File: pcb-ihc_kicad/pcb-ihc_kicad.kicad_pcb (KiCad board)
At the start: 2 copper layers, 100 x 160 mm, 76 parts, among them J1 D-IN with pullup, J10 D-IN with pulldown, J11 2x N-Mosfet, J2 Screw_Terminal_01x01, J3 Screw_Terminal_01x01, J4 Screw_Terminal_01x01, J5 Screw_Terminal_01x01, J6 Screw_Terminal_01x01, J7 Screw_Terminal_01x01, J8 Screw_Terminal_01x01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

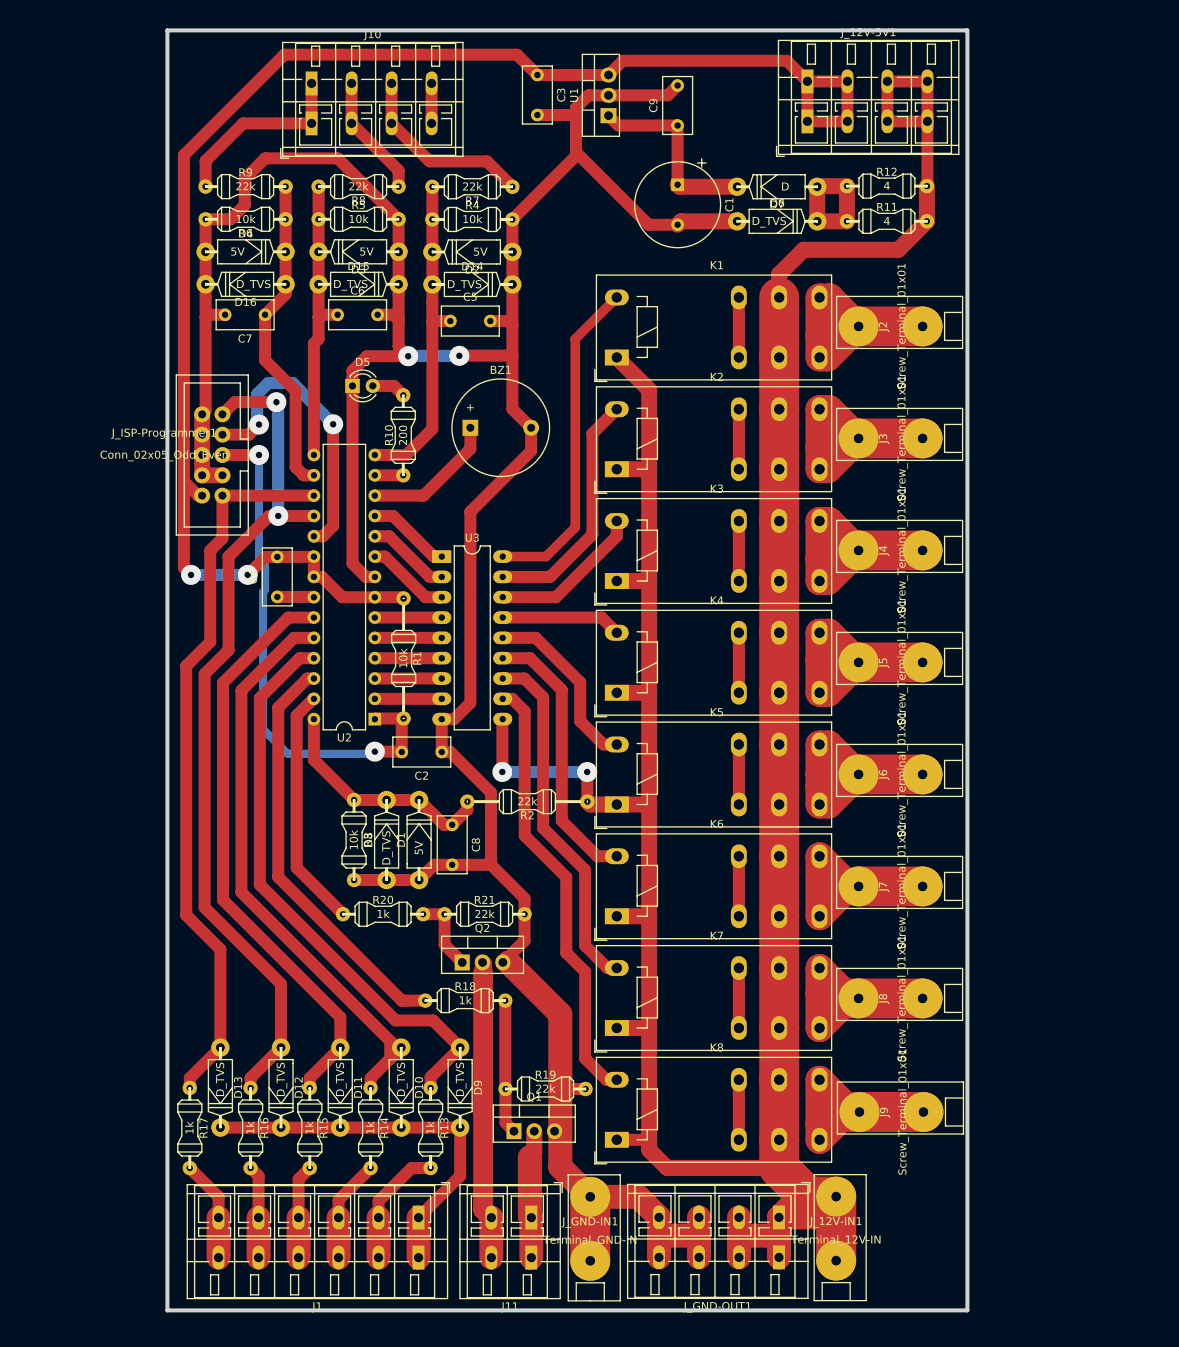
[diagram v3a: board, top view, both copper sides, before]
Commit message: Optimize routing and layout
- fix track width on several locations (1.5 to 2mm)
- minor changes in routing
- move relays closer together
- add additional 12V input terminal
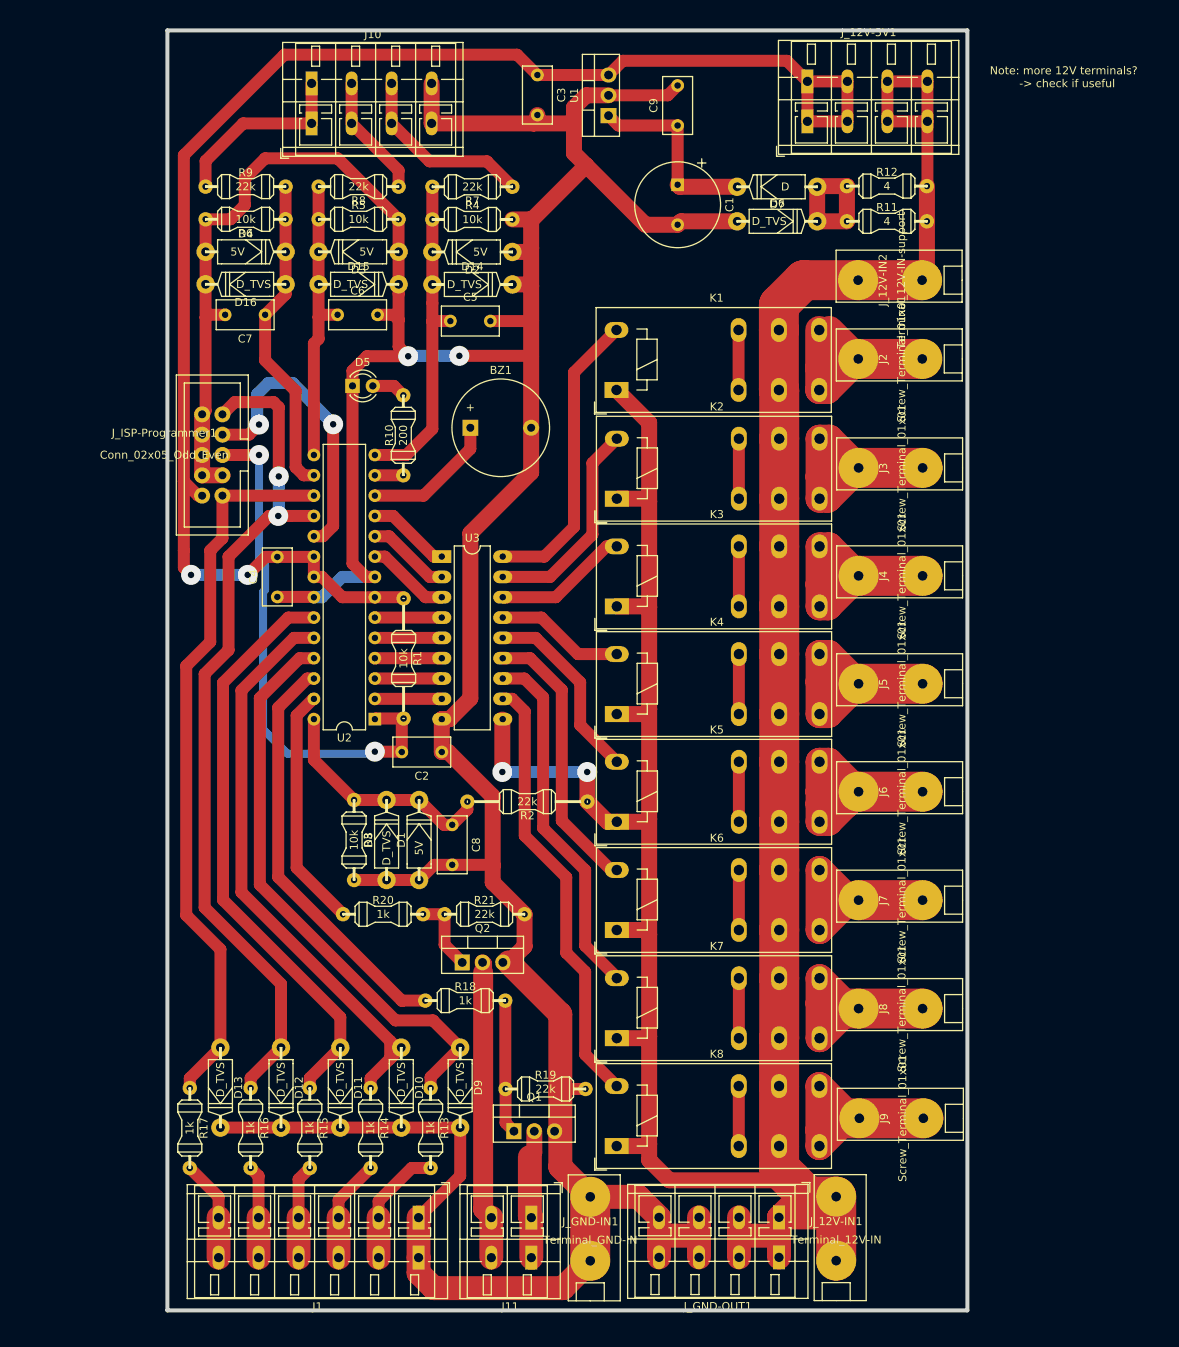
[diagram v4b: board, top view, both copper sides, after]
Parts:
- added J_12V-IN2: Terminal_12V-IN-support, custom_footprints:my_KlemmeWago2604-single, F.Cu at (159.3, 46.2)
- moved J2 4.06 mm to (159.4, 56.1)
- moved K1 4.06 mm to (121.1, 59.9)
- moved J3 3.68 mm to (159.4, 69.7)
- moved K2 3.68 mm to (121.2, 73.5)
- moved K3 3.18 mm to (121.2, 87.0)
- moved J4 3.17 mm to (159.4, 83.2)
- moved J5 2.67 mm to (159.4, 96.7)
- moved K4 2.67 mm to (121.2, 100.5)
- moved J6 2.16 mm to (159.4, 110.2)
- moved K5 2.16 mm to (121.2, 113.9)
- moved J7 1.72 mm to (159.4, 123.7)
- moved K6 1.72 mm to (121.2, 127.4)
- moved J8 1.27 mm to (159.4, 137.3)
- moved K7 1.27 mm to (121.2, 141.0)
- moved J9 0.78 mm to (159.5, 151.0)
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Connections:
- J10 pad 4: unconnected-(J10-Pad4) -> GND
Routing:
- net GND: track 447.6 -> 510.0 mm
- net unconnected-(J10-Pad4): track 5.00 -> 0.00 mm
- net Net-(K1-PadA2): track 41.5 -> 37.3 mm
- net Net-(K2-PadA2): track 30.3 -> 26.7 mm
- net Net-(K3-PadA2): track 19.3 -> 16.9 mm
- net +12V: track 382.4 -> 383.8 mm
- net Net-(J2-Pad1): track 33.7 -> 32.5 mm
- net Net-(K5-PadA2): track 22.6 -> 23.8 mm
- net Net-(K4-PadA2): track 15.0 -> 16.1 mm
- net Net-(K6-PadA2): track 34.1 -> 34.8 mm
- net Net-(K7-PadA2): track 44.4 -> 44.9 mm
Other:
- board text added: "Note: more 12V terminals? -> check if useful"

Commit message: Add terminal descriptions, Clean up schematic
- Add detailed terminal/connector descriptions (e.g. which uC pin)
- Positioned labels in layout outside of pcb
- cleanup in schematic reorder groups, fix boxes...
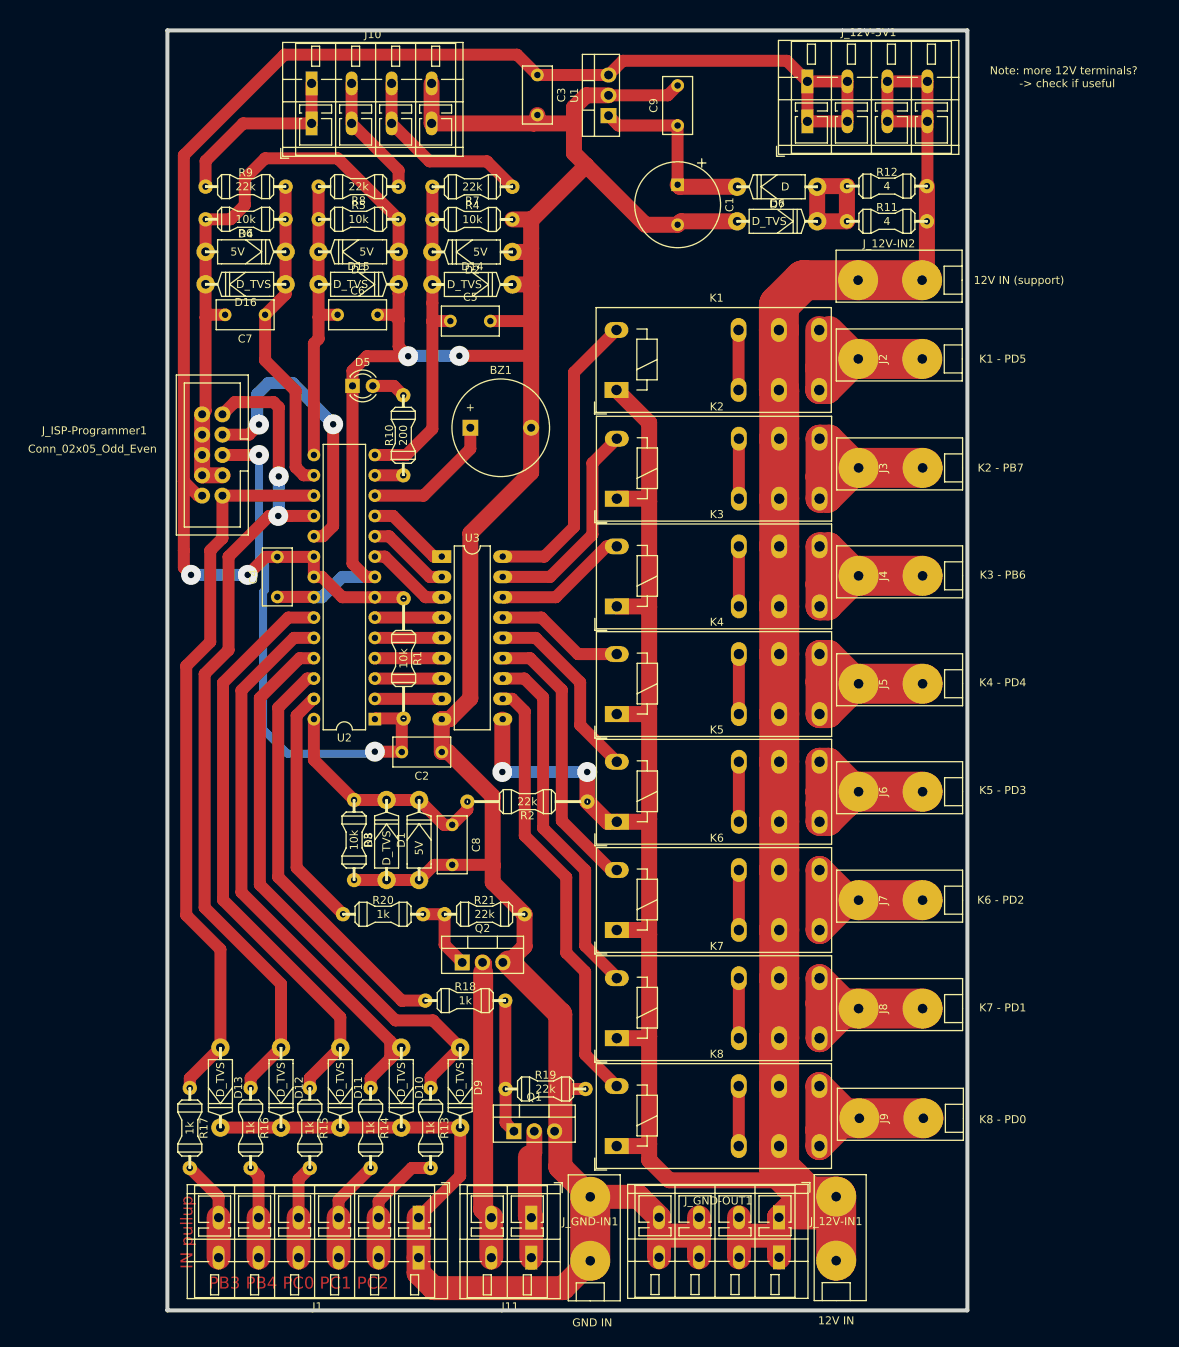
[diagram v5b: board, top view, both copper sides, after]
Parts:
- BZ1: value Buzzer -> Buzzer - PD6
- D5: value LED -> LED - PD7
- J2: value Screw_Terminal_01x01 -> K1 - PD5
- J3: value Screw_Terminal_01x01 -> K2 - PB7
- J4: value Screw_Terminal_01x01 -> K3 - PB6
- J5: value Screw_Terminal_01x01 -> K4 - PD4
- J6: value Screw_Terminal_01x01 -> K5 - PD3
- J7: value Screw_Terminal_01x01 -> K6 - PD2
- J8: value Screw_Terminal_01x01 -> K7 - PD1
- J9: value Screw_Terminal_01x01 -> K8 - PD0
- J_12V-5V1: value Screw_Terminal_01x04 -> 2x 5V out, 2 x 12V out
- J_12V-IN1: value Terminal_12V-IN -> 12V IN
- J_12V-IN2: value Terminal_12V-IN-support -> 12V IN (support)
- J_GND-IN1: value Terminal_GND-IN -> GND IN
- J_GND-OUT1: value Screw_Terminal_01x04 -> 2x GND out, 2x 12V out
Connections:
- net /PB5 (SCK) renamed /ISP-SCK
- net /PC6 Reset renamed /ISP-Reset
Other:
- board text added: "IN pullup"
- board text added: "PB3 PB4 PC0 PC1 PC2"

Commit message: Swap Layers Front/Back Tracks
Noticed in 3d viewer that tracks were on the same side as components...
swaped F.Cu and B.Cu using " Edit -> Swap layers ". Now tracks are on
the other side...
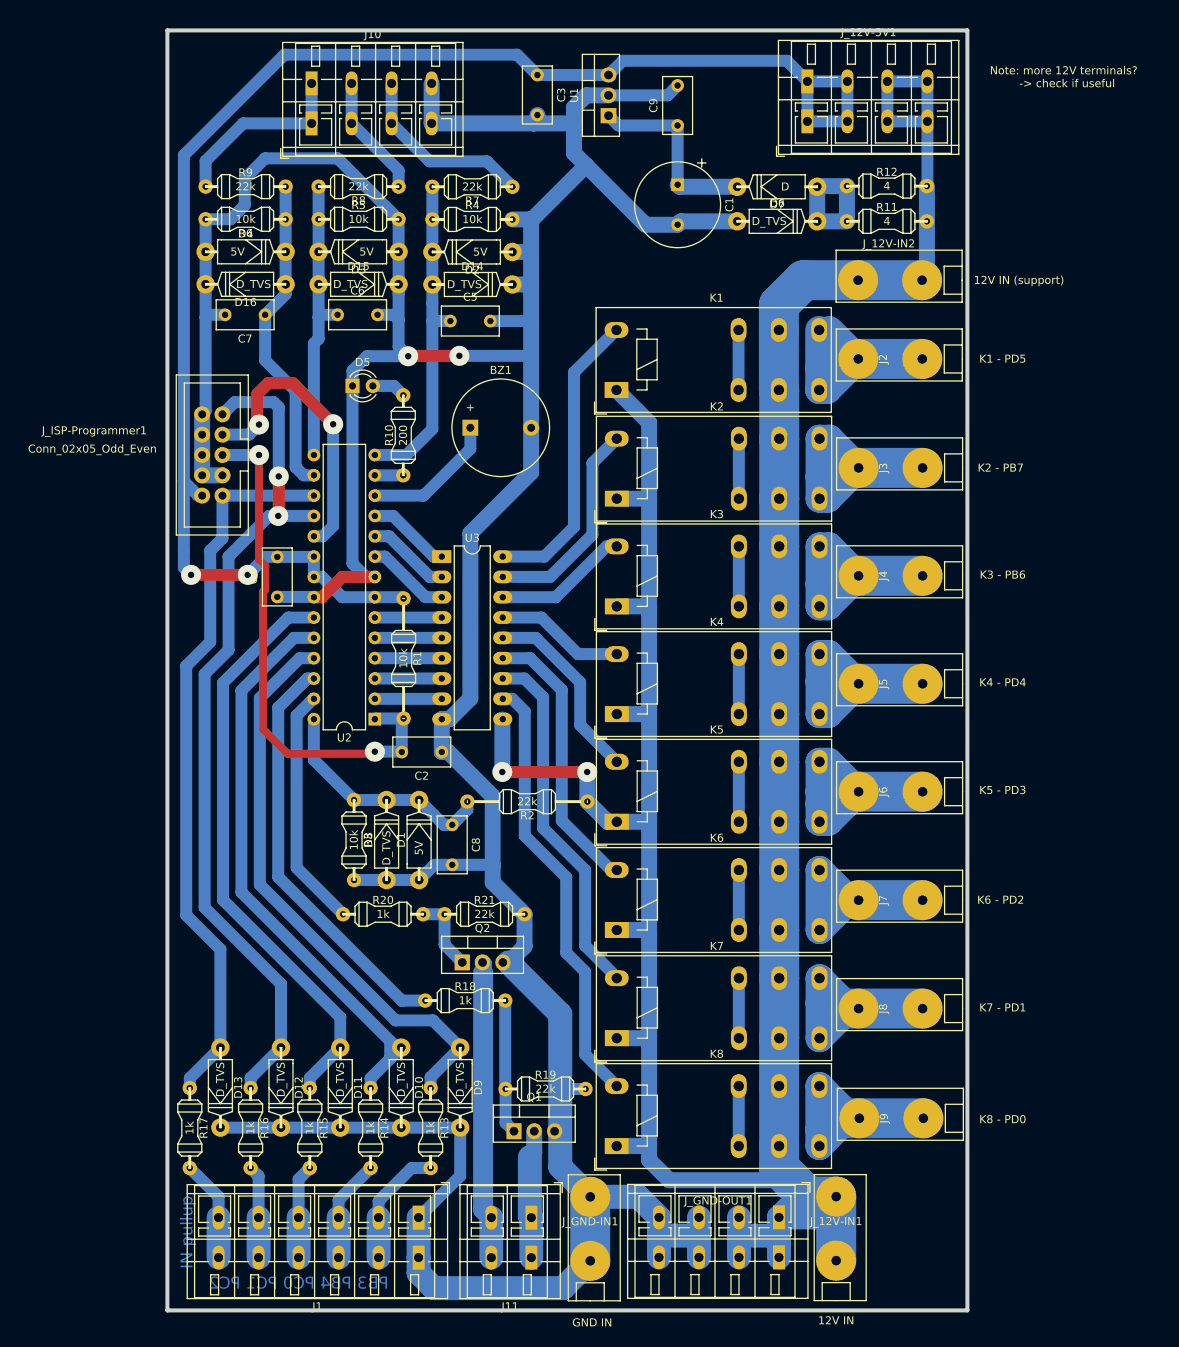
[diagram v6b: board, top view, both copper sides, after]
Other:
- board text added: "TEST text PC1"
